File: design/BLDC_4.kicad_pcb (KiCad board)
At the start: 4 copper layers, 50 x 100 mm, 140 parts, among them P1 HALL/Encoder, P10 EXT_I2C, P11 OLED, P12 BRAKE, P13 BUTTONS, P14 EXTENSION, P2 SWD, P3 5V_OUT, P4 IN+, P5 IN-, P6 MOTOR1, P7 MOTOR2, P8 GND_OUT, P9 MOTOR3, Q1 IRFS7530, Q2 IRFS7530, Q3 IRFS7530, Q4 IRFS7530, Q5 IRFS7530, Q6 IRFS7530, U1 STM32F40X_LQFP64, U2 TC2117, U3 DRV8302, U4 LSM6DS3, U5 MICROSD, U6 BLUETOOTH_SPP-CA, X1 MINI-USB-SHIELD-32005-201, X2 8MHz 10ppm

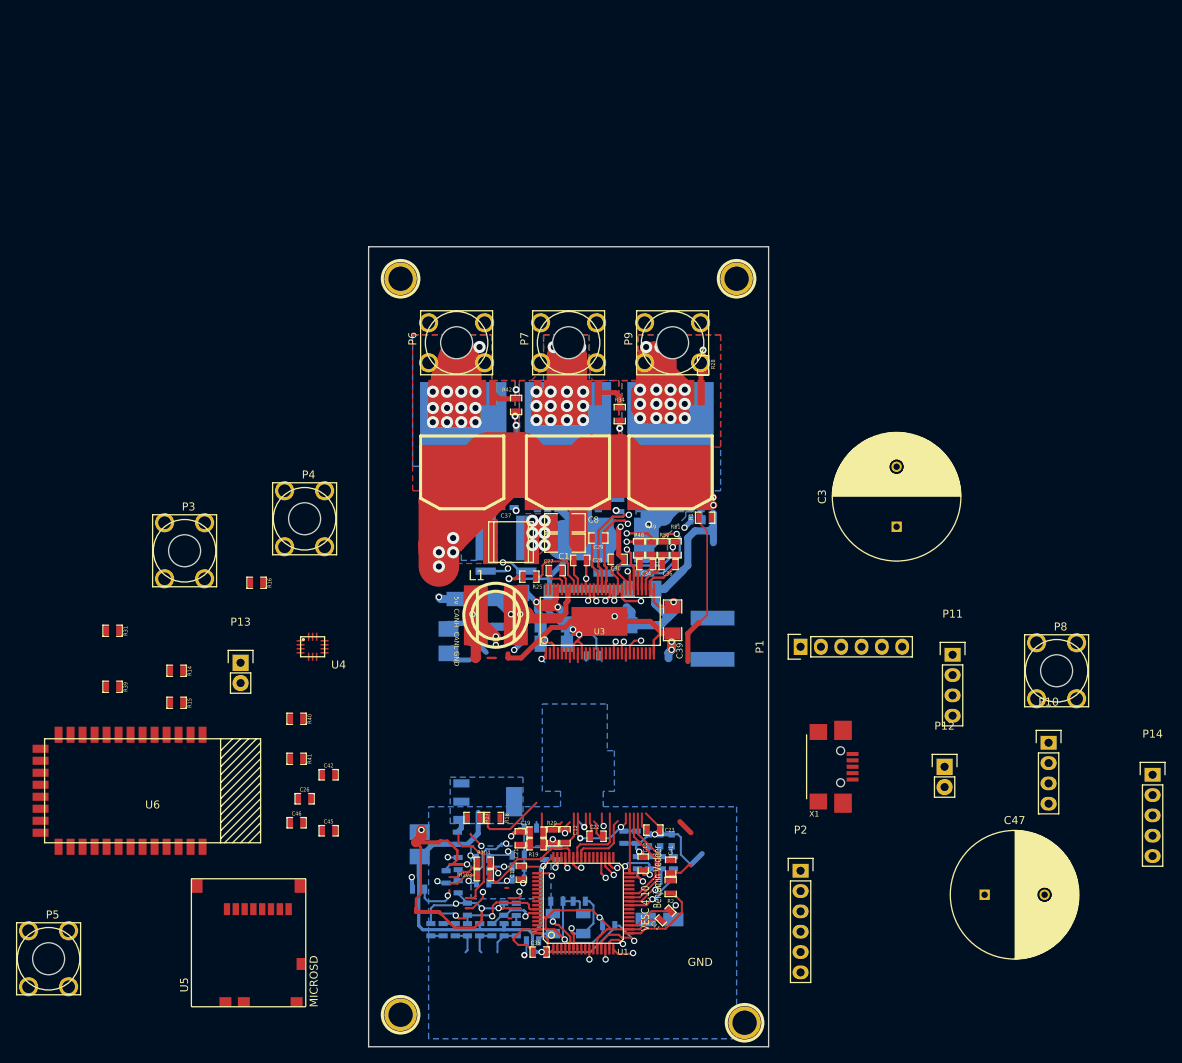
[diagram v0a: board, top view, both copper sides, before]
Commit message: Relayout to more compact version, update to KiCad 7
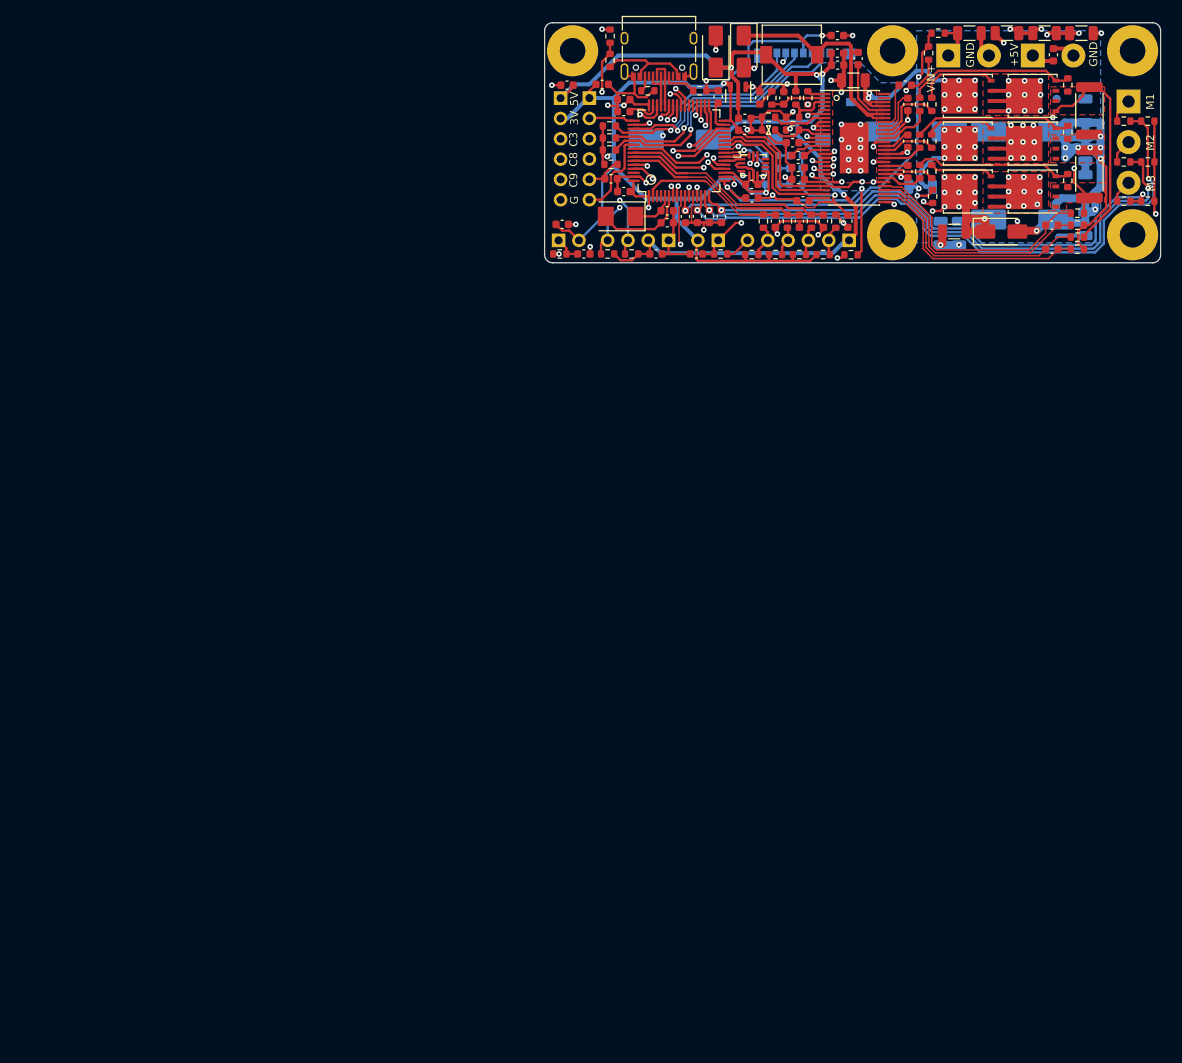
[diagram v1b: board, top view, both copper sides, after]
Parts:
- removed 1PIN (x2): P***, 1pin
- removed 1PIN (x2): P***, Connect:1pin
- removed C10, C14, C31, C35: 2.2u, CRF1:SMD-0603_c
- removed C25: 100u, w_smd_cap:c_tant_B
- removed G***: oshw_silkscreen-back_3mm, oshw_silkscreen-back_3mm
- removed P10: EXT_I2C, Pin_Headers:Pin_Header_Straight_1x04
- removed P3: 5V_OUT, KEYS7775:KEYS7775
- removed P4: IN+, KEYS7775:KEYS7775
- removed P5: IN-, KEYS7775:KEYS7775
- removed P6: MOTOR1, KEYS7775:KEYS7775
- removed P7: MOTOR2, KEYS7775:KEYS7775
- removed P8: GND_OUT, KEYS7775:KEYS7775
- removed P9: MOTOR3, KEYS7775:KEYS7775
- removed R103, R104: 22R, CRF1:SMD-0603_r
- removed R25: 1M, CRF1:SMD-0603_r
- removed U2: TC2117, CRF1:SOT-223
- removed X1: MINI-USB-SHIELD-32005-201, CRF1:USB-UX60R-MB-5ST
- removed X2: 8MHz 10ppm, CRF1:Crystal_5x3mm
- added C48: 4.7uF, Capacitor_SMD:C_0603_1608Metric, F.Cu at (105.2, 57.7)
- added C50: 1uF,100V, Capacitor_SMD:C_1206_3216Metric, B.Cu at (165.6, 75.1)
- added C501: 4.7nF, Capacitor_SMD:C_0603_1608Metric, F.Cu at (120.1, 74.2)
- added C502: 4.7nF, Capacitor_SMD:C_0603_1608Metric, F.Cu at (118.6, 74.2)
- added C503: 4.7nF, Capacitor_SMD:C_0603_1608Metric, F.Cu at (117.1, 74.2)
- added C53: 1uF,100V, Capacitor_SMD:C_1206_3216Metric, F.Cu at (136.6, 57.2)
- added C54: 1uF,100V, Capacitor_SMD:C_1206_3216Metric, B.Cu at (165.6, 61.0)
- added C55: 1uF,100V, Capacitor_SMD:C_1206_3216Metric, B.Cu at (149.8, 76.3)
- added C56: 1uF,100V, Capacitor_SMD:C_1206_3216Metric, B.Cu at (147.5, 76.3)
- added C57: 100uF,63V, Capacitor_SMD:CP_Elec_10x10.5, B.Cu at (157.7, 74.6)
- added C58: 100uF,63V, Capacitor_SMD:CP_Elec_10x10.5, B.Cu at (144.4, 63.6)
- added C59: 100uF,63V, Capacitor_SMD:CP_Elec_10x10.5, B.Cu at (157.7, 63.6)
- added C60: 4.7uF, Capacitor_SMD:C_0603_1608Metric, F.Cu at (111.9, 78.9)
- added C61: 4.7uF, Capacitor_SMD:C_0603_1608Metric, F.Cu at (100.8, 57.8)
- added C62: 100nF, Capacitor_SMD:C_0603_1608Metric, F.Cu at (143.1, 57.8)
- added D7: SMAJ48, Diode_SMD:D_SMA, F.Cu at (155.1, 76.1)
- added H1: M3, MountingHole:MountingHole_3.2mm_M3_Pad, F.Cu at (171.5, 53.5)
- added H2: M3, MountingHole:MountingHole_3.2mm_M3_Pad, F.Cu at (171.5, 76.5)
- added H3: M3, MountingHole:MountingHole_3.2mm_M3_Pad, F.Cu at (141.5, 76.5)
- added H4: M3, MountingHole:MountingHole_3.2mm_M3_Pad, F.Cu at (141.5, 53.5)
- added H5: M3, MountingHole:MountingHole_3.2mm_M3_Pad, F.Cu at (101.5, 53.5)
- added J1: Motor, TerminalBlock:TerminalBlock_bornier-3_P5.08mm, B.Cu at (171.0, 59.8)
- added J2: 5V_OUT, TerminalBlock:TerminalBlock_bornier-2_P5.08mm, B.Cu at (159.0, 54.1)
- added J3: 40V_IN, TerminalBlock:TerminalBlock_bornier-2_P5.08mm, B.Cu at (148.5, 54.1)
- added J401: USB_C_Receptacle_USB2.0, Connector_USB:USB_C_Receptacle_XKB_U262-16XN-4BVC11, F.Cu at (112.3, 53.0)
- added R401: 4k7, Resistor_SMD:R_0603_1608Metric, F.Cu at (117.4, 58.5)
- added R402: 4k7, Resistor_SMD:R_0603_1608Metric, F.Cu at (110.9, 58.5)
- added R403: 4k7, Resistor_SMD:R_0603_1608Metric, F.Cu at (106.2, 51.7)
- added R404: 4k7, Resistor_SMD:R_0603_1608Metric, F.Cu at (106.2, 54.7)
- added R405: 4k7, Resistor_SMD:R_0603_1608Metric, F.Cu at (106.3, 67.7)
- added R44: 10k, Resistor_SMD:R_0603_1608Metric, F.Cu at (129.0, 63.4)
- added R5: N/A, Resistor_SMD:R_0603_1608Metric, F.Cu at (126.0, 63.4)
- added Y1: 8MHz, Crystal:Crystal_SMD_5032-2Pin_5.0x3.2mm, F.Cu at (107.5, 74.2)
- C1, C8: value 10u,50V -> 4.7uF; footprint CRF1:SMD-1206 -> Capacitor_SMD:C_0603_1608Metric
- C11, C12, C13, C41: value 2.2u -> 100nF; footprint CRF1:SMD-0603_c -> Capacitor_SMD:C_0603_1608Metric
- C15, C38: value 15p -> 22pF; footprint CRF1:SMD-0603_c -> Capacitor_SMD:C_0603_1608Metric; moved to F.Cu
- C16, C17, C18, C20, C24, C52: value 2.2u -> 4.7uF; footprint CRF1:SMD-0603_c -> Capacitor_SMD:C_0603_1608Metric; moved to F.Cu
- C19: value 120p -> 22pF; footprint CRF1:SMD-0603_c -> Capacitor_SMD:C_0603_1608Metric
- C2, C32: value 100n -> 100nF; footprint CRF1:SMD-0603_c -> Capacitor_SMD:C_0603_1608Metric; moved to F.Cu
- C21: value 6.8n -> 4.7nF; footprint CRF1:SMD-0603_c -> Capacitor_SMD:C_0603_1608Metric
- C22: value 22n -> 100nF; footprint CRF1:SMD-0603_c -> Capacitor_SMD:C_0603_1608Metric
- C23, C26, C46: value 2.2u -> 4.7uF; footprint CRF1:SMD-0603_c -> Capacitor_SMD:C_0603_1608Metric
- C27: value 100n -> 100nF; footprint CRF1:SMD-0603_c -> Capacitor_SMD:C_0603_1608Metric
- C28, C29, C30: value 220n -> 100nF; footprint CRF1:SMD-0603_c -> Capacitor_SMD:C_0603_1608Metric
- C3, C47: value 680µF -> 4.7uF; footprint Capacitors_ThroughHole:C_Radial_D16_L25_P7.5 -> Capacitor_SMD:C_0603_1608Metric
- C33: value 100u -> 470µF; footprint w_smd_cap:c_tant_B -> Capacitor_SMD:CP_Elec_10x10.5
- C34, C36: value 2.2n -> 4.7nF; footprint CRF1:SMD-0603_c -> Capacitor_SMD:C_0603_1608Metric
- C37: value 15u,100V -> 1uF,100V; footprint w_smd_cap:c_2220 -> Capacitor_SMD:C_1206_3216Metric
- C39, C44, C49, C9: value 10u,50V -> 1uF,100V; footprint CRF1:SMD-1206 -> Capacitor_SMD:C_1206_3216Metric
- C4, C5, C6, C7: value 4n7 -> 4.7nF; footprint CRF1:SMD-0603_c -> Capacitor_SMD:C_0603_1608Metric; moved to F.Cu
- C40, C43: value 10u,50V -> 1uF,100V; footprint CRF1:SMD-1206 -> Capacitor_SMD:C_1206_3216Metric; moved to F.Cu
- C42, C45: footprint CRF1:SMD-0603_c -> Capacitor_SMD:C_0603_1608Metric
- C51: value 15u, 100v -> 1uF,100V; footprint w_smd_cap:c_2220 -> Capacitor_SMD:C_1206_3216Metric; moved to F.Cu
- D1, D2, D3: footprint LEDs:LED-0603 -> LED_SMD:LED_0603_1608Metric
- D4: value DIODESCH -> Schottky; footprint Diodes_SMD:SMA_Handsoldering -> Diode_SMD:D_SMA; moved to F.Cu
- D5: value TVS 5V -> SMAJ5; footprint w_smd_diode:do214ac -> Diode_SMD:D_SMA; moved to F.Cu
- L1: footprint w_smd_inductors:inductor_smd_8x5mm -> Inductor_SMD:L_7.3x7.3_H4.5
- P1, P2: footprint Pin_Headers:Pin_Header_Straight_1x06 -> Connector_PinHeader_2.54mm:PinHeader_1x06_P2.54mm_Vertical; moved to B.Cu
- P11: footprint Pin_Headers:Pin_Header_Straight_1x04 -> Connector_PinHeader_2.54mm:PinHeader_1x04_P2.54mm_Vertical; moved to B.Cu
- P12, P13: footprint Pin_Headers:Pin_Header_Straight_1x02 -> Connector_PinHeader_2.54mm:PinHeader_1x02_P2.54mm_Vertical; moved to B.Cu
- P14: footprint Pin_Headers:Pin_Header_Straight_1x05 -> Connector_PinHeader_2.54mm:PinHeader_1x06_P2.54mm_Vertical; moved to B.Cu
- Q1, Q3, Q5: value IRFS7530 -> BSC030N08NS5; footprint CRF1:D2PAK-7-GDS -> Package_TO_SOT_SMD:TDSON-8-1
- Q2, Q4, Q6: value IRFS7530 -> BSC030N08NS5; footprint CRF1:D2PAK-7-GDS -> Package_TO_SOT_SMD:TDSON-8-1; moved to F.Cu
- R1, R2, R20, R22, R28, R34, R37, R38, R39, R40, R41, R42, R48, R49, R50, R51: footprint CRF1:SMD-0603_r -> Resistor_SMD:R_0603_1608Metric
- R10, R8, R9: value 10k -> 4k7; footprint CRF1:SMD-0603_r -> Resistor_SMD:R_0603_1608Metric; moved to F.Cu
- R11, R12, R13, R21, R23, R24, R26, R27, R29, R3, R30, R32, R33, R35, R36, R4, R43, R46: footprint CRF1:SMD-0603_r -> Resistor_SMD:R_0603_1608Metric; moved to F.Cu
- R14, R15, R16, R31: value 2k -> 2k2; footprint CRF1:SMD-0603_r -> Resistor_SMD:R_0603_1608Metric
- R17: value 18k -> 12k; footprint CRF1:SMD-0603_r -> Resistor_SMD:R_0603_1608Metric
- R18: value 3k3 -> 2k2; footprint CRF1:SMD-0603_r -> Resistor_SMD:R_0603_1608Metric
- R19: value 15k -> 10k; footprint CRF1:SMD-0603_r -> Resistor_SMD:R_0603_1608Metric
- R53, R54: value SHUNT -> 5m; footprint CRF1:WSLP2726 -> Resistor_SMD:R_2512_6332Metric; moved to F.Cu
- R6: value 0R -> 4k7; footprint CRF1:SMD-0603_r -> Resistor_SMD:R_0603_1608Metric; moved to F.Cu
- R7: value 10k -> 2k2; footprint CRF1:SMD-0603_r -> Resistor_SMD:R_0603_1608Metric; moved to F.Cu
- U1: footprint CRF1:lqfp64_pad_mod -> Package_QFP:LQFP-64_10x10mm_P0.5mm
- U3: footprint CRF1:TSSOP-56-PP -> Package_SO:HTSSOP-56-1EP_6.1x14mm_P0.5mm_EP3.61x6.35mm
- U5: footprint microsd:MOLEX_502570-0893 -> Connector_Card:microSD_HC_Molex_104031-0811; moved to B.Cu
- U6: value BLUETOOTH_SPP-CA -> XC6206PxxxMR; footprint bluetooth_spp-ca:bluetooth_spp-ca -> Package_TO_SOT_SMD:SOT-23-3
- moved U5 126.6 mm to (130.5, 59.2), turned to 180 degrees
- moved R32 122.1 mm to (170.4, 62.3)
- moved R33 120.9 mm to (173.4, 62.3)
- moved R3 119.9 mm to (147.2, 51.3), turned to 180 degrees
- moved R4 119.6 mm to (146.0, 53.8)
- moved R26 119.5 mm to (170.4, 67.4)
- moved C46 119.4 mm to (134.6, 51.6), turned to 180 degrees
- moved R27 118.2 mm to (173.4, 67.4)
- moved R23 117.0 mm to (170.4, 72.3)
- moved R24 115.7 mm to (173.4, 72.3)
- moved U6 113.6 mm to (122.2, 59.1), turned to -90 degrees
- moved P14 112.4 mm to (100.0, 59.4), turned to 180 degrees
- moved D5 108.7 mm to (119.4, 53.6), turned to 90 degrees
- moved C47 105.4 mm to (161.6, 54.0), turned to 90 degrees
- moved C4 102.8 mm to (135.9, 74.8)
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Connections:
- net /MCU/ADC_TEMP renamed TEMPERATURE
- net Net-(C34-Pad1) renamed /Mosfet driver/SN1
- net Net-(C34-Pad2) renamed /Mosfet driver/SP1
- net Net-(C36-Pad1) renamed /Mosfet driver/SN2
- net Net-(C36-Pad2) renamed /Mosfet driver/SP2
- C1 pad 1: GND -> +5V
- C1 pad 2: V_SUPPLY -> GND
- C20 pad 2: Net-(C20-Pad2) -> /Mosfet driver/DVDD
- C27 pad 1: Net-(C27-Pad1) -> Net-(D4-K)
- C3 pad 1: V_SUPPLY -> +5V
- C37 pad 1: GND -> V_SUPPLY
- C37 pad 2: V_SUPPLY -> GND
- C4 pad 2: /Filters/TEMP_IN -> /Filters/WHEEL_OUT
- C40 pad 1: GND -> V_SUPPLY
- C40 pad 2: V_SUPPLY -> GND
- C47 pad 1: V_SUPPLY -> +5V
- C51 pad 1: GND -> V_SUPPLY
- C51 pad 2: V_SUPPLY -> GND
- C52 pad 2: Net-(C20-Pad2) -> /Mosfet driver/DVDD
- C8 pad 1: GND -> +5V
- C8 pad 2: V_SUPPLY -> GND
- C9 pad 1: GND -> V_SUPPLY
- C9 pad 2: V_SUPPLY -> GND
- D1 pad 1: Net-(D1-Pad1) -> GND
- D1 pad 2: GND -> Net-(D1-A)
- D2 pad 1: Net-(D2-Pad1) -> GND
- D2 pad 2: GND -> Net-(D2-A)
- D3 pad 1: Net-(D3-Pad1) -> GND
- D3 pad 2: GND -> Net-(D3-A)
- D4 pad 1: GND -> Net-(D4-K)
- D4 pad 2: Net-(C27-Pad1) -> GND
- D5 pad 1: GND -> +5V
- D5 pad 2: +5V -> GND
- L1 pad 1: Net-(C27-Pad1) -> Net-(D4-K)
- P1 pad 2: /Filters/TEMP_IN -> /Filters/WHEEL_IN
- P14 pad 1: VCC -> +5V
- P14 pad 2: Net-(P14-Pad2) -> VCC
- P14 pad 3: Net-(P14-Pad3) -> /MCU/PC3
- P14 pad 4: Net-(P14-Pad4) -> /MCU/PC8
- P14 pad 5: GND -> /MCU/PC9
- R16 pad 1: VCC -> +5V
- R22 pad 1: Net-(D3-Pad1) -> Net-(D3-A)
- R28 pad 1: Net-(Q1-PadG) -> Net-(Q1-G)
- R29 pad 1: Net-(Q2-PadG) -> Net-(Q2-G)
- R30 pad 2: Net-(Q2-PadG) -> Net-(Q2-G)
- R31 pad 1: VCC -> +5V
- R34 pad 1: Net-(Q3-PadG) -> Net-(Q3-G)
- R35 pad 1: Net-(Q4-PadG) -> Net-(Q4-G)
- R36 pad 1: /Mosfet driver/H1_LOW -> Net-(Q4-G)
- R36 pad 2: Net-(Q4-PadG) -> GND
- R37 pad 1: Net-(D1-Pad1) -> Net-(D1-A)
- R38 pad 1: Net-(D2-Pad1) -> Net-(D2-A)
- R42 pad 1: Net-(Q5-PadG) -> Net-(Q5-G)
- R43 pad 1: Net-(Q6-PadG) -> Net-(Q6-G)
- R46 pad 2: Net-(Q6-PadG) -> Net-(Q6-G)
- R48 pad 1: /Mosfet driver/SH1_A -> /Mosfet driver/H3_LOW
- R49 pad 1: /Mosfet driver/SH1_B -> GND
- R50 pad 1: /Mosfet driver/SH2_A -> /Mosfet driver/H1_LOW
- R51 pad 1: /Mosfet driver/SH2_B -> GND
- R53 pad 1: GND -> /Mosfet driver/H1_LOW
- R53 pad 2: /Mosfet driver/H1_LOW -> GND
- R6 pad 1: Net-(R6-Pad1) -> /Filters/WHEEL_IN
- R6 pad 2: +5V -> /Filters/WHEEL_OUT
- R7 pad 1: /Filters/TEMP_IN -> /Filters/WHEEL_IN
- U1 pad 11: Net-(P14-Pad2) -> /MCU/PC3
- U1 pad 28: Net-(U1-Pad28) -> unconnected-(U1-PB2-BOOT1-Pad28)
- U1 pad 3: Net-(U1-Pad3) -> unconnected-(U1-PC14-OSC32_IN-Pad3)
- U1 pad 37: BLUETOOTH_RX -> unconnected-(U1-PC6-Pad37)
- U1 pad 38: BLUETOOTH_TX -> unconnected-(U1-PC7-Pad38)
- U1 pad 39: Net-(P14-Pad3) -> /MCU/PC8
- U1 pad 4: Net-(U1-Pad4) -> unconnected-(U1-PC15-OSC32_OUT-Pad4)
- U1 pad 40: Net-(P14-Pad4) -> /MCU/PC9
- U1 pad 60: GND -> /MCU/BOOT0
- U1 pad 62: Net-(U1-Pad62) -> unconnected-(U1-PB9-Pad62)
- U1 pad 8: /Filters/TEMP_IN -> /Filters/WHEEL_OUT
- U3 pad 11: Net-(C20-Pad2) -> Net-(U3-OC_ADJ)
- U3 pad 23: Net-(C20-Pad2) -> /Mosfet driver/DVDD
- U3 pad 4: Net-(U3-Pad4) -> unconnected-(U3-PWRGD-Pad4)
- U3 pad 5: Net-(U3-Pad5) -> unconnected-(U3-OCTW-Pad5)
- U3 pad 50: Net-(C27-Pad1) -> Net-(D4-K)
- U3 pad 51: Net-(C27-Pad1) -> Net-(D4-K)
- U3 pad 55: Net-(U3-Pad55) -> unconnected-(U3-EN_BUCK-Pad55)
- U3 pad 56: Net-(U3-Pad56) -> unconnected-(U3-SS_TR-Pad56)
- U3 pad 9: VCC -> GND
- U4 pad 10: Net-(U4-Pad10) -> unconnected-(U4-OCS-Pad10)
- U4 pad 9: Net-(U4-Pad9) -> unconnected-(U4-INT2-Pad9)
- U6 pad 1: BLUETOOTH_TX -> GND
- U6 pad 2: BLUETOOTH_RX -> VCC
- U6 pad 3: (no net) -> +5V
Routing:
- net V_SUPPLY: track 214.3 -> 63.5 mm, vias 10 -> 35
- net +5V: track 38.5 -> 164.7 mm
- net /Mosfet driver/H3_VS: track 166.9 -> 50.1 mm, vias 18 -> 10
- net /Mosfet driver/H1_VS: track 149.6 -> 52.4 mm, vias 18 -> 10
- net /Mosfet driver/H2_VS: track 145.0 -> 53.9 mm, vias 17 -> 10
- net GND: track 346.5 -> 258.5 mm, vias 26 -> 59
- net (no net): track 50.3 -> 0.00 mm, vias 5 -> 0
- net /MCU/SENS3: track 30.2 -> 80.0 mm
- net /MCU/SENS2: track 28.6 -> 72.1 mm
- net /MCU/SENS1: track 26.3 -> 66.3 mm
- net /MCU/FAULT: track 0.00 -> 35.8 mm, vias 0 -> 2
- net /Mosfet driver/M_H3: track 40.9 -> 6.42 mm, vias 2 -> 0
- net /MCU/EN_GATE: track 0.00 -> 34.0 mm, vias 0 -> 2
- net SPI3_SDCARD_CS: track 0.00 -> 33.5 mm, vias 0 -> 1
- net SPI3_MOSI: track 0.00 -> 31.5 mm, vias 0 -> 1
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- added copper zone on F.Cu, net /Mosfet driver/H1_LOW
- added copper zone on In2.Cu, net /Mosfet driver/H1_VS
- added copper zone on In2.Cu, net /Mosfet driver/H2_VS
- added copper zone on F.Cu, net /Mosfet driver/H3_LOW
- added copper zone on In2.Cu, net /Mosfet driver/H3_VS
- added copper zone on In1.Cu, net GND
- added copper zone on B.Cu, net V_SUPPLY
- removed copper zone on B.Cu, net /Mosfet driver/H1_LOW
- removed copper zone on B.Cu, net /Mosfet driver/H1_VS
- removed copper zone on GND, net /Mosfet driver/H1_VS
- removed copper zone on GND2, net /Mosfet driver/H1_VS
- removed copper zone on B.Cu, net /Mosfet driver/H2_VS
- removed copper zone on GND, net /Mosfet driver/H2_VS
- removed copper zone on GND2, net /Mosfet driver/H2_VS
- removed copper zone on B.Cu, net /Mosfet driver/H3_LOW
- removed copper zone on B.Cu, net /Mosfet driver/H3_VS
- removed copper zone on GND, net /Mosfet driver/H3_VS
- removed copper zone on GND2, net /Mosfet driver/H3_VS
- removed copper zone on GND, net GND
- removed copper zone on GND2, net GND
- removed copper zone on B.Cu, net VCC
- removed copper zone on F.Cu, net V_SUPPLY
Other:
- board size 50 x 100 mm -> 77 x 30 mm
- net class Default removed
- board text added: "+5V"
- board text added: "1"
- board text added: "2"
- board text added: "3"
- board text added: "3V"
- board text added: "48V+"
- board text added: "5V"
- board text added: "BRAKE"
- board text added: "Based on VESC 4.10"
- board text added: "C3"
- board text added: "C8"
- board text added: "C9"
- board text added: "E-bike Controller JPA 2023"
- board text added: "G"
- board text added: "HALL1"
- board text added: "HALL2"
- board text added: "HALL3"
- board text added: "M1"
- board text added: "M2"
- board text added: "M3"
- board text added: "NRST"
- board text added: "Optional MicroSD"
- board text added: "SCL"
- board text added: "SDA"
- board text added: "SWC"
- board text added: "SWD"
- board text added: "SWO"
- board text added: "UI_BTN"
- board text added: "VCC"
- board text added: "VIN+"
- board text added: "WHEEL"
- board text removed: "5v"
- board text removed: "Benjamin Vedder"
- board text removed: "CANH"
- board text removed: "CANL"
- board text removed: "VESC 4.10"
- board text removed: "vedder.se"

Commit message: Update README, add FreeCAD design of mounting
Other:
- board text removed: "2"
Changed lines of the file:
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@@
     )
     (pad_to_mask_clearance 0)
-    (aux_axis_origin 68 170)
+    (aux_axis_origin 98 50)
     (pcbplotparams
       (layerselection 0x00010f0_80000007)
@@
       (rotate (xyz 0 0 0))
     )
+    (model ":KICAD7_3DMODEL_DIR:Connector_USB.3dshapes/USB_C_Receptacle_GCT_USB4105-xx-A_16P_TopMnt_Horizontal.step"
+      (offset (xyz 0 0 0))
+      (scale (xyz 1 1 1))
+      (rotate (xyz 0 0 0))
+    )
   )
   (footprint "Capacitor_SMD:C_0603_1608Metric" (layer "F.Cu")
@@
       (rotate (xyz 0 0 0))
     )
+    (model ":KICAD7_3DMODEL_DIR:TerminalBlock_Phoenix.3dshapes/TerminalBlock_Phoenix_PT-1,5-2-5.0-H_1x02_P5.00mm_Horizontal.step"
+      (offset (xyz 0 0 0))
+      (scale (xyz 1 1 1))
+      (rotate (xyz 0 0 0))
+    )
   )
   (footprint "TerminalBlock:TerminalBlock_bornier-2_P5.08mm" (layer "B.Cu")
@@
       (rotate (xyz 0 0 0))
     )
+    (model ":KICAD7_3DMODEL_DIR:TerminalBlock_Phoenix.3dshapes/TerminalBlock_Phoenix_PT-1,5-2-5.0-H_1x02_P5.00mm_Horizontal.step"
+      (offset (xyz 0 0 0))
+      (scale (xyz 1 1 1))
+      (rotate (xyz 0 0 0))
+    )
   )
   (footprint "Capacitor_SMD:CP_Elec_10x10.5" (layer "B.Cu")
@@
       (rotate (xyz 0 0 0))
     )
+    (model ":KICAD7_3DMODEL_DIR:TerminalBlock_Phoenix.3dshapes/TerminalBlock_Phoenix_PT-1,5-3-5.0-H_1x03_P5.00mm_Horizontal.wrl"
+      (offset (xyz 0 0 0))
+      (scale (xyz 1 1 1))
+      (rotate (xyz 0 0 0))
+    )
   )
   (footprint "Capacitor_SMD:C_1206_3216Metric" (layer "B.Cu")
@@
   (gr_line (start 175 51) (end 175 79)
     (stroke (width 0.15) (type default)) (layer "Edge.Cuts"))
-  (gr_text "2" (at 95.75 160.5) (layer "In1.Cu")
-    (effects (font (size 2 2) (thickness 0.3)))
-  )
   (gr_text "NRST" (at 108.9 70.2) (layer "B.SilkS")
     (effects (font (size 1 1) (thickness 0.15)) (justify left bottom mirror))
